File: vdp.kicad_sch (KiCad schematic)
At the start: 1 part, among them IC6 D92046GD001

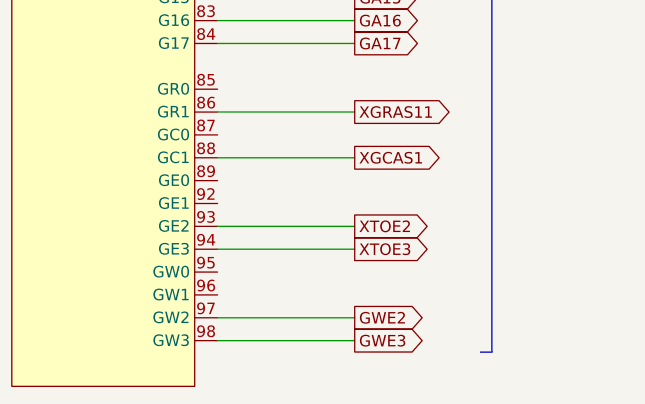
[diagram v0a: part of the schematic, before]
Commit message: schematic: fix IC6
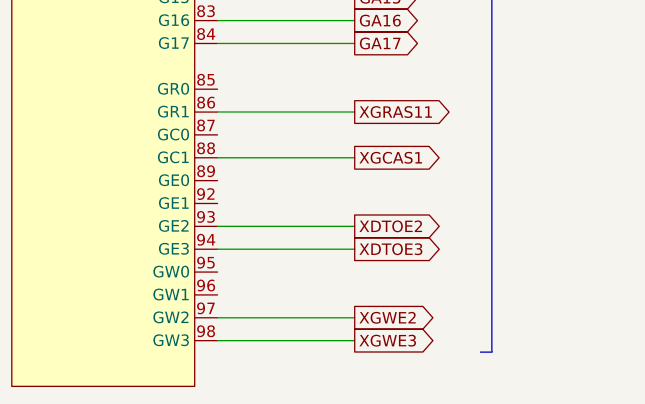
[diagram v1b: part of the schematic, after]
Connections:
- net GWE2 renamed XGWE2
- net GWE3 renamed XGWE3
- net XTOE2 renamed XDTOE2
- net XTOE3 renamed XDTOE3
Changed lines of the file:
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@@
     )
   )
-  (global_label "XTOE3" (shape output) (at 99.06 120.65 0) (fields_autoplaced)
+  (global_label "XDTOE3" (shape output) (at 99.06 120.65 0) (fields_autoplaced)
     (effects (font (size 1.27 1.27)) (justify left))
-    (property "Intersheetrefs" "${INTERSHEET_REFS}" (at 107.9113 120.65 0)
+    (property "Intersheetrefs" "${INTERSHEET_REFS}" (at 109.1813 120.65 0)
       (effects (font (size 1.27 1.27)) (justify left) hide)
     )
   )
-  (global_label "GWE3" (shape output) (at 99.06 130.81 0) (fields_autoplaced)
+  (global_label "XGWE3" (shape output) (at 99.06 130.81 0) (fields_autoplaced)
     (effects (font (size 1.27 1.27)) (justify left))
-    (property "Intersheetrefs" "${INTERSHEET_REFS}" (at 107.1251 130.81 0)
+    (property "Intersheetrefs" "${INTERSHEET_REFS}" (at 108.3346 130.81 0)
       (effects (font (size 1.27 1.27)) (justify left) hide)
     )
   )
-  (global_label "XTOE2" (shape output) (at 99.06 118.11 0) (fields_autoplaced)
+  (global_label "XDTOE2" (shape output) (at 99.06 118.11 0) (fields_autoplaced)
     (effects (font (size 1.27 1.27)) (justify left))
-    (property "Intersheetrefs" "${INTERSHEET_REFS}" (at 107.9113 118.11 0)
+    (property "Intersheetrefs" "${INTERSHEET_REFS}" (at 109.1813 118.11 0)
       (effects (font (size 1.27 1.27)) (justify left) hide)
     )
@@
     )
   )
-  (global_label "GWE2" (shape output) (at 99.06 128.27 0) (fields_autoplaced)
+  (global_label "XGWE2" (shape output) (at 99.06 128.27 0) (fields_autoplaced)
     (effects (font (size 1.27 1.27)) (justify left))
-    (property "Intersheetrefs" "${INTERSHEET_REFS}" (at 107.1251 128.27 0)
+    (property "Intersheetrefs" "${INTERSHEET_REFS}" (at 108.3346 128.27 0)
       (effects (font (size 1.27 1.27)) (justify left) hide)
     )

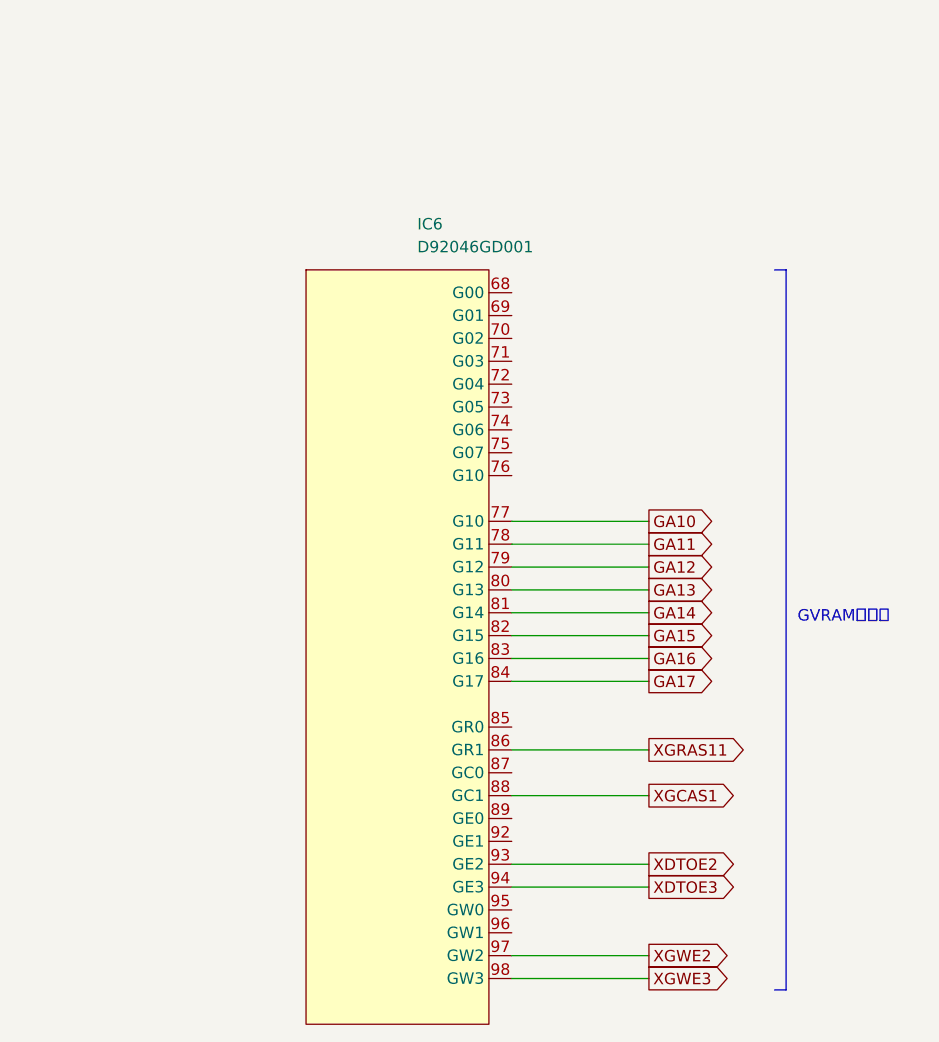
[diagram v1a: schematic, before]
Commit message: schematic: add lines from IC9 to GVRAM1-4
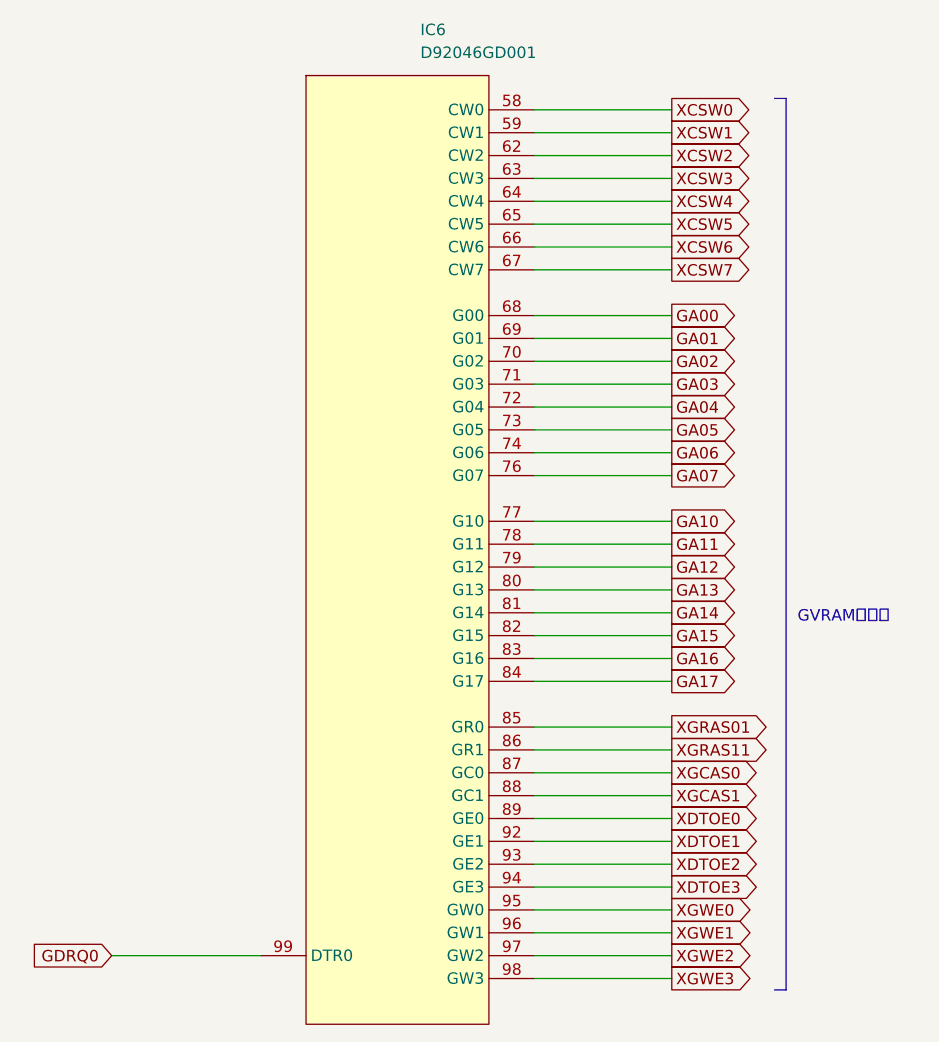
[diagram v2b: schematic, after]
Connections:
- net GA00: now reaches IC6.68 (G00)
- net GA01: now reaches IC6.69 (G01)
- net GA02: now reaches IC6.70 (G02)
- net GA03: now reaches IC6.71 (G03)
- net GA04: now reaches IC6.72 (G04)
- net GA05: now reaches IC6.73 (G05)
- net GA06: now reaches IC6.74 (G06)
- net GA07: now reaches IC6.76 (G07)
- net XGRAS01: now reaches IC6.85 (GR0)
- net XGCAS0: now reaches IC6.87 (GC0)
- net XDTOE0: now reaches IC6.89 (GE0)
- net XDTOE1: now reaches IC6.92 (GE1)
- net XGWE0: now reaches IC6.95 (GW0)
- net XGWE1: now reaches IC6.96 (GW1)
- new net GDRQ0: IC6.99 (DTR0)
- new net XCSW0: IC6.58 (CW0)
- new net XCSW1: IC6.59 (CW1)
- new net XCSW2: IC6.62 (CW2)
- new net XCSW3: IC6.63 (CW3)
- new net XCSW4: IC6.64 (CW4)
- new net XCSW5: IC6.65 (CW5)
- new net XCSW6: IC6.66 (CW6)
- new net XCSW7: IC6.67 (CW7)
